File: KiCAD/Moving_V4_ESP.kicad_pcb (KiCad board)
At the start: 2 copper layers, 38 x 63 mm, 48 parts, among them J1 Vin_1, J2 Vin_2, J3 Power_SW, J4 USB_B_Micro, J5 MOTOR_R, J6 Motor_L, SW1 SW_Reset, U1 CH340X, U2 UZ1085L-33-TN3-R, U3 ESP32-WROOM-32, U4 ITR8307-S17-TR8, U5 ITR8307-S17-TR8, U6 ITR8307-S17-TR8, U7 CP2119LDTR, U8 CP2119LDTR

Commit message: Revのテキストを更新
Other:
- board text added: "ESP Mini PF Base Circuit 38 x 63 Rev 0.2"
- board text removed: "ESP Mini PF Base Circuit 38 x 63 Rev 0.1"
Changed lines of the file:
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@@
     (effects (font (size 1 1) (thickness 0.15)) (justify left bottom))
   )
-  (gr_text "ESP Mini PF Base Circuit\n38 x 63\nRev 0.1" (at 108 106) (layer "F.SilkS")
+  (gr_text "ESP Mini PF Base Circuit\n38 x 63\nRev 0.2" (at 108 106) (layer "F.SilkS")
     (effects (font (size 1 1) (thickness 0.15)) (justify left bottom))
   )

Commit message: 主要部品をロック
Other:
- board text added: "locked"
- board text removed: "ESP Mini PF Base Circuit 38 x 63 Rev 0.2"

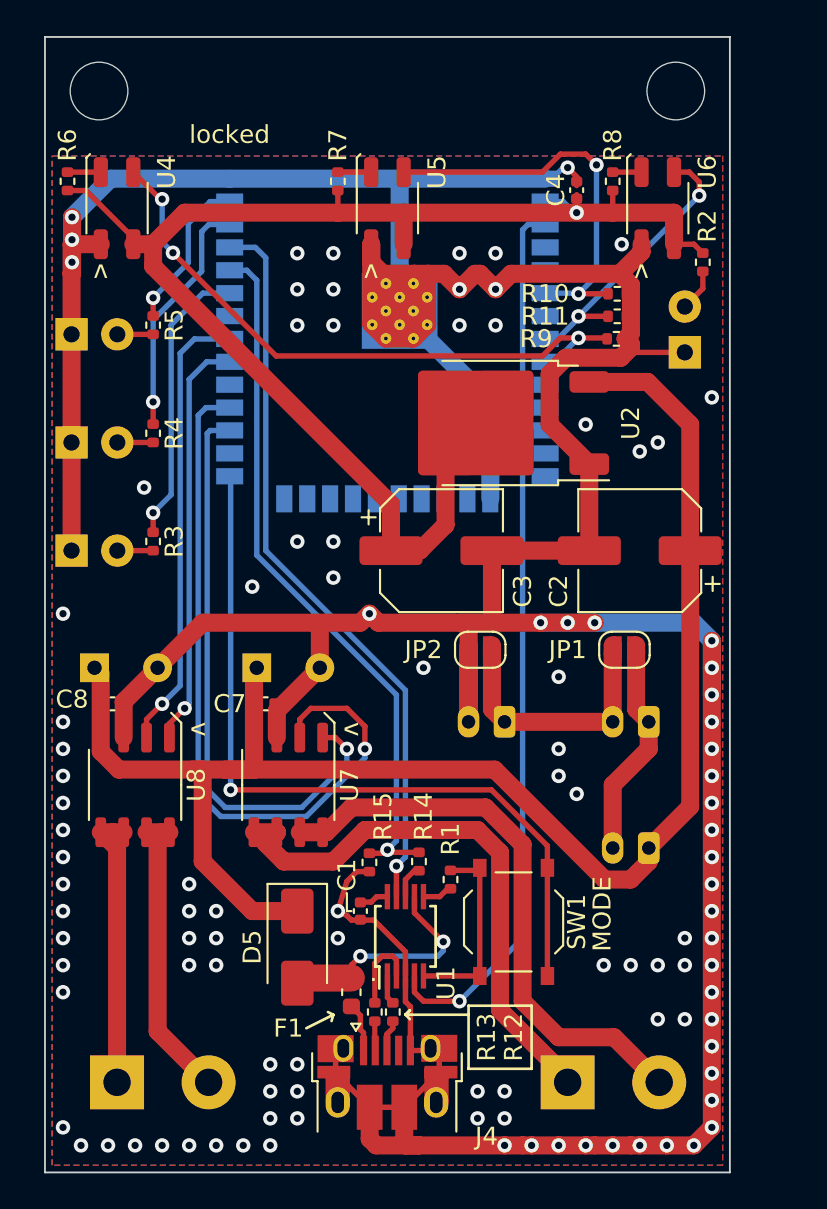
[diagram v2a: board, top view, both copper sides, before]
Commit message: 部品を仮配置
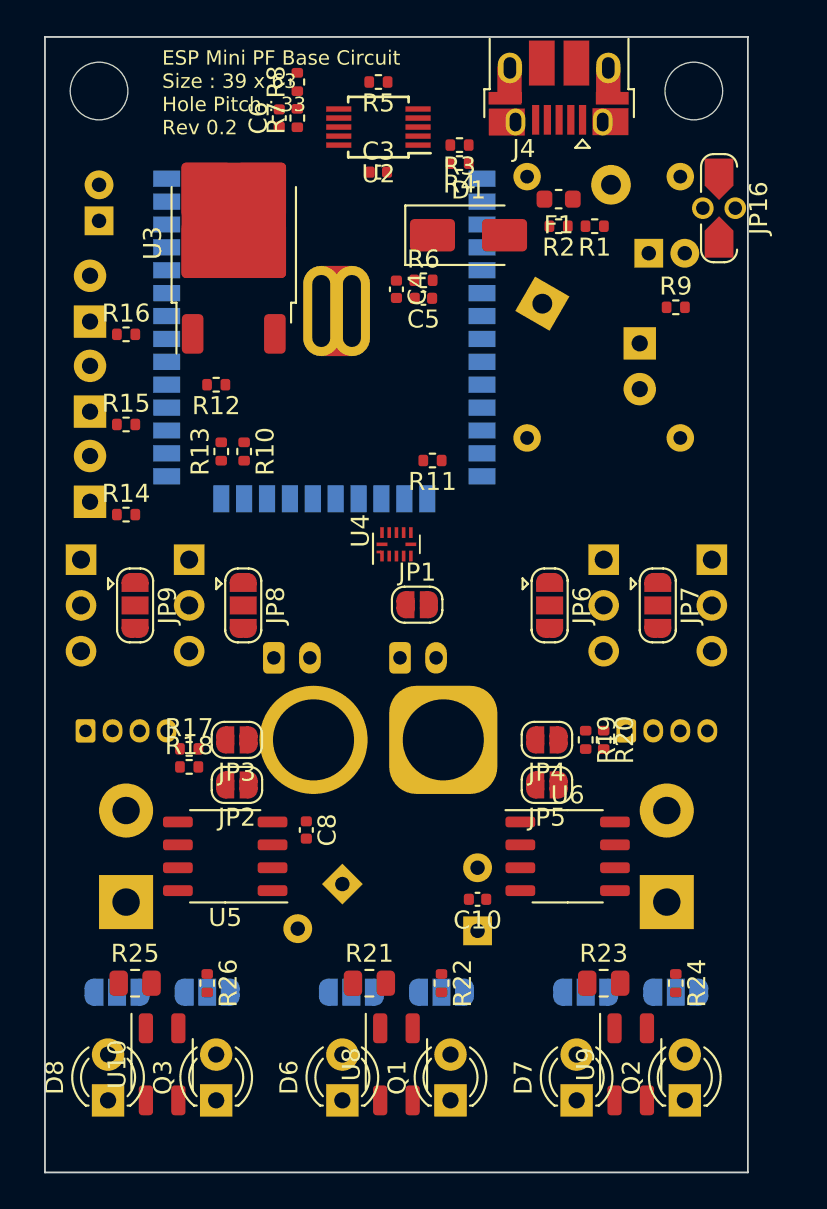
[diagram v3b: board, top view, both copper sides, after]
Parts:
- removed SW1: SW_Reset, Button_Switch_SMD:SW_Push_1P1T_XKB_TS-1187A
- removed the U7 at (113.5, 141.5)
- added C10: 0.1u, Capacitor_SMD:C_0402_1005Metric, F.Cu at (124.0, 147.8)
- added C9: 470u, Capacitor_THT:CP_Radial_D8.0mm_P3.50mm, B.Cu at (124.0, 149.6)
- added D6: U4_ALT1, LED_THT:LED_D3.0mm, F.Cu at (116.5, 159.0)
- added D7: U4_ALT1, LED_THT:LED_D3.0mm, F.Cu at (129.5, 159.0)
- added D8: U4_ALT1, LED_THT:LED_D3.0mm, F.Cu at (103.5, 159.0)
- added J10: IO27_GPIO1, Connector_PinHeader_2.54mm:PinHeader_1x03_P2.54mm_Vertical, B.Cu at (137.0, 129.0)
- added J11: IO32_GPIO2, Connector_PinHeader_2.54mm:PinHeader_1x03_P2.54mm_Vertical, B.Cu at (108.0, 129.0)
- added J12: IO5_GPIO3(PU), Connector_PinHeader_2.54mm:PinHeader_1x03_P2.54mm_Vertical, B.Cu at (102.0, 129.0)
- added J7: MOTOR_L, TerminalBlock:TerminalBlock_bornier-2_P5.08mm, B.Cu at (104.5, 148.0)
- added J8: MOTOR_R, TerminalBlock:TerminalBlock_bornier-2_P5.08mm, B.Cu at (134.5, 148.0)
- added J9: IO4_GPIO0, Connector_PinHeader_2.54mm:PinHeader_1x03_P2.54mm_Vertical, B.Cu at (131.0, 129.0)
- added JP10: LED_SEL1, Jumper:SolderJumper-3_P1.3mm_Open_RoundedPad1.0x1.5mm, B.Cu at (117.0, 153.0)
- added JP11: PT_SEL1, Jumper:SolderJumper-3_P1.3mm_Open_RoundedPad1.0x1.5mm, B.Cu at (122.0, 153.0)
- added JP12: LED_SEL1, Jumper:SolderJumper-3_P1.3mm_Open_RoundedPad1.0x1.5mm, B.Cu at (130.0, 153.0)
- added JP13: PT_SEL1, Jumper:SolderJumper-3_P1.3mm_Open_RoundedPad1.0x1.5mm, B.Cu at (135.0, 153.0)
- added JP14: LED_SEL1, Jumper:SolderJumper-3_P1.3mm_Open_RoundedPad1.0x1.5mm, B.Cu at (104.0, 153.0)
- added JP15: PT_SEL1, Jumper:SolderJumper-3_P1.3mm_Open_RoundedPad1.0x1.5mm, B.Cu at (109.0, 153.0)
- added JP16: Reset, YY_Common:SolderJumper-2_TVAF06-A020B-R_COMPATIBLE, F.Cu at (137.4, 109.5)
- added JP17: USB_Vs, Diode_THT:D_DO-41_SOD81_P7.62mm_Horizontal, B.Cu at (127.6, 114.8)
- added JP3: L2_PU, Jumper:SolderJumper-2_P1.3mm_Open_RoundedPad1.0x1.5mm, F.Cu at (110.7, 139.0)
- added JP4: R1_PU, Jumper:SolderJumper-2_P1.3mm_Open_RoundedPad1.0x1.5mm, F.Cu at (127.8, 139.0)
- added JP5: R2_PU, Jumper:SolderJumper-2_P1.3mm_Open_RoundedPad1.0x1.5mm, F.Cu at (127.8, 141.5)
- added JP6: Vs_SEL0, Jumper:SolderJumper-3_P1.3mm_Open_RoundedPad1.0x1.5mm, F.Cu at (128.0, 131.5)
- added JP7: Vs_SEL1, Jumper:SolderJumper-3_P1.3mm_Open_RoundedPad1.0x1.5mm, F.Cu at (134.0, 131.5)
- added JP8: Vs_SEL2, Jumper:SolderJumper-3_P1.3mm_Open_RoundedPad1.0x1.5mm, F.Cu at (111.0, 131.5)
- added JP9: Vs_SEL3, Jumper:SolderJumper-3_P1.3mm_Open_RoundedPad1.0x1.5mm, F.Cu at (105.0, 131.5)
- added Q1: U4_ALT2, LED_THT:LED_D3.0mm, F.Cu at (122.5, 159.0)
- added Q2: U4_ALT2, LED_THT:LED_D3.0mm, F.Cu at (135.5, 159.0)
- added Q3: U4_ALT2, LED_THT:LED_D3.0mm, F.Cu at (109.5, 159.0)
- added R16: 560, Resistor_SMD:R_0402_1005Metric, F.Cu at (104.5, 116.5)
- added R17: 1k, Resistor_SMD:R_0402_1005Metric, F.Cu at (108.0, 139.5)
- added R18: 1k, Resistor_SMD:R_0402_1005Metric, F.Cu at (108.0, 140.5)
- added R19: 1k, Resistor_SMD:R_0402_1005Metric, F.Cu at (130.0, 139.0)
- added R20: 1k, Resistor_SMD:R_0402_1005Metric, F.Cu at (131.0, 139.0)
- added R21: 50, Resistor_SMD:R_0805_2012Metric, F.Cu at (118.0, 152.5)
- added R22: 1k, Resistor_SMD:R_0402_1005Metric, F.Cu at (122.0, 152.5)
- added R23: 50, Resistor_SMD:R_0805_2012Metric, F.Cu at (131.0, 152.5)
- added R24: 1k, Resistor_SMD:R_0402_1005Metric, F.Cu at (135.0, 152.5)
- added R25: 50, Resistor_SMD:R_0805_2012Metric, F.Cu at (105.0, 152.5)
- added R26: 1k, Resistor_SMD:R_0402_1005Metric, F.Cu at (109.0, 152.5)
- added U10: ITR8307-S17-TR8, OptoDevice:Everlight_ITR1201SR10AR, F.Cu at (106.5, 157.0)
- added U3: UZ1085L-33-TN3-R, Package_TO_SOT_SMD:TO-252-2, F.Cu at (110.5, 111.4)
- added U9: ITR8307-S17-TR8, OptoDevice:Everlight_ITR1201SR10AR, F.Cu at (132.5, 157.0)
- C1: value 0.1u -> 22u; footprint Capacitor_SMD:C_0402_1005Metric -> Capacitor_THT:CP_Radial_D5.0mm_P2.00mm; moved to B.Cu
- C2: footprint Capacitor_SMD:CP_Elec_6.3x5.4 -> Capacitor_THT:CP_Radial_D5.0mm_P2.00mm; moved to B.Cu
- C3: value 22u -> 0.1u; footprint Capacitor_SMD:CP_Elec_6.3x5.4 -> Capacitor_SMD:C_0402_1005Metric
- C5: value 470u -> 10u; footprint Capacitor_THT:CP_Radial_D8.0mm_P3.50mm -> Capacitor_SMD:C_0402_1005Metric; moved to F.Cu
- C6: value 470u -> 20p; footprint Capacitor_THT:CP_Radial_D8.0mm_P3.50mm -> Capacitor_SMD:C_0402_1005Metric; moved to F.Cu
- C7: value 0.1u -> 470u; footprint Capacitor_SMD:C_0402_1005Metric -> Capacitor_THT:CP_Radial_D8.0mm_P3.50mm; moved to B.Cu
- D1: value LED_POWER -> CDBA240LL-HF; footprint LED_THT:LED_D3.0mm -> Diode_SMD:D_SMA; moved to F.Cu
- D2: value LED_R -> LED_POWER
- D3: value LED_Y -> LED_R
- D4: value LED_G -> LED_Y
- D5: value CDBA240LL-HF -> LED_G; footprint Diode_SMD:D_SMA -> LED_THT:LED_D3.0mm; moved to B.Cu
- J2: value Vin_2 -> Power_SW
- J3: value Power_SW -> Vin_XT; footprint Connector_JST:JST_PH_B2B-PH-K_1x02_P2.00mm_Vertical -> Connector_AMASS:AMASS_XT60-M_1x02_P7.20mm_Vertical
- J5: value MOTOR_R -> Encorder_L; footprint TerminalBlock:TerminalBlock_bornier-2_P5.08mm -> YY_Common:JST_ZH_B4B-ZH-A_1x04_P1.50mm_Vertical
- J6: value Motor_L -> Encorder_R; footprint TerminalBlock:TerminalBlock_bornier-2_P5.08mm -> YY_Common:JST_ZH_B4B-ZH-A_1x04_P1.50mm_Vertical
- JP1: value Vin_2_DIisable -> Power_SW_DIisable
- JP2: value Power_SW_DIisable -> L1_PU
- R1: value 4.7k -> 18k
- R12, R13: value 22 -> 1k
- R15, R9: value 1k -> 560
- R2: value 560 -> 2k
- R3, R4: value 560 -> 22
- R5: value 560 -> 4.7k
- R6, R8: value 150 -> 1k
- R7: value 150 -> 560
- U1: value CH340X -> CN39033A; footprint Package_SO:MSOP-10_3x3mm_P0.5mm -> YY_Common:DCDC_Conv_CN39033A; moved to B.Cu
- U2: value UZ1085L-33-TN3-R -> CH340X; footprint Package_TO_SOT_SMD:TO-252-2 -> Package_SO:MSOP-10_3x3mm_P0.5mm
- U4: value ITR8307-S17-TR8 -> TXB0104RUT; footprint OptoDevice:Everlight_ITR1201SR10AR -> Package_DFN_QFN:Texas_R-PUQFN-N12
- U5, U6: value ITR8307-S17-TR8 -> CP3119MDTR; footprint OptoDevice:Everlight_ITR1201SR10AR -> Package_SO:SOP-8_3.9x4.9mm_P1.27mm
- U7: renamed from U3; footprint RF_Module:ESP32-WROOM-32 -> YY_Common:ESP32-WROOM-32_39P-TH
- U8: value CP2119LDTR -> ITR8307-S17-TR8; footprint Package_SO:SOP-8_3.9x4.9mm_P1.27mm -> OptoDevice:Everlight_ITR1201SR10AR
- moved J4 56.0 mm to (128.5, 102.8), turned to 180 degrees
- moved F1 45.5 mm to (128.5, 109.0), turned to 180 degrees
- moved C1 39.9 mm to (133.5, 112.0), turned to 0 degrees
- moved R1 37.1 mm to (130.5, 110.5), turned to 180 degrees
- moved U5 37.1 mm to (110.0, 145.5), turned to 180 degrees
- moved U1 36.6 mm to (131.0, 115.0)
- moved D5 36.6 mm to (102.5, 115.8), turned to 90 degrees
- moved U6 36.3 mm to (129.0, 145.5)
- moved R12 36.2 mm to (109.5, 119.3), turned to 180 degrees
- moved C2 35.1 mm to (103.0, 110.2), turned to 90 degrees
- moved D2 33.6 mm to (133.0, 117.0), turned to -90 degrees
- moved R13 32.2 mm to (109.8, 123.0)
- moved C6 32.2 mm to (113.0, 104.5), turned to 90 degrees
- moved R15 27.8 mm to (104.5, 121.5), turned to 0 degrees
- moved R3 27.8 mm to (123.0, 106.0), turned to 180 degrees
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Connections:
- C1 pad 1: Net-(U1-V3) -> +5V
- C2 pad 1: /Vin -> +3.3V
- C3 pad 1: +3.3V -> Net-(U2-V3)
- C5 pad 1: /Vin -> /EN
- C6 pad 1: /Vin -> /Tx(USB->ESP)
- C6 pad 2: GND -> Net-(U7-RXD0/IO3)
- D1 pad 1: GND -> +5V
- D1 pad 2: Net-(D1-A) -> /USB 5V_F
- D2 pad 1: GND -> Net-(D2-K)
- D2 pad 2: Net-(D2-A) -> +3.3V
- D3 pad 1: GND -> Net-(D3-K)
- D3 pad 2: Net-(D3-A) -> /LED_R
- D4 pad 1: GND -> Net-(D4-K)
- D4 pad 2: Net-(D4-A) -> /LED_Y
- D5 pad 1: /Vin -> Net-(D5-K)
- D5 pad 2: /USB 5V_F -> /LED_G
- J2 pad 2: /P_in2- -> GND
- J3 pad 1: /P_in2- -> GND
- J3 pad 2: GND -> /Vin
- J5 pad 1: /P_MOT_R2 -> +5V
- J5 pad 2: /P_MOT_R1 -> Net-(J5-Pin_2)
- J6 pad 1: /P_MOT_L2 -> +5V
- J6 pad 2: /P_MOT_L1 -> Net-(J6-Pin_2)
- JP1 pad 2: /P_in2- -> GND
- JP2 pad 1: /P_in2- -> Net-(J5-Pin_2)
- JP2 pad 2: GND -> Net-(JP2-B)
- R1 pad 1: Net-(U1-~{CTS}) -> /Vin
- R1 pad 2: Net-(U1-TNOW/~{DTR}) -> /Vs_monitor
- R10 pad 1: /SENSOR_2 -> +3.3V
- R10 pad 2: GND -> /MTDO
- R11 pad 1: /SENSOR_3 -> /MTDI
- R12 pad 1: /D+ -> +3.3V
- R12 pad 2: Net-(U1-UD+) -> /Debug Log
- R13 pad 1: /D- -> /DL Boot
- R13 pad 2: Net-(U1-UD-) -> GND
- R14 pad 1: /Tx(USB->ESP) -> Net-(D3-K)
- R14 pad 2: Net-(U3-RXD0/IO3) -> GND
- R15 pad 1: Net-(U3-RXD0/IO3) -> Net-(D4-K)
- R2 pad 1: +3.3V -> /Vs_monitor
- R2 pad 2: Net-(D1-A) -> GND
- R3 pad 1: /LED_R -> /D+
- R3 pad 2: Net-(D2-A) -> Net-(U2-UD+)
- R4 pad 1: /LED_Y -> /D-
- R4 pad 2: Net-(D3-A) -> Net-(U2-UD-)
- R5 pad 1: /LED_G -> /IO_0
- R5 pad 2: Net-(D4-A) -> Net-(U2-TNOW/~{DTR})
- R6 pad 1: Net-(U4-A) -> +3.3V
- R6 pad 2: +3.3V -> /EN
- R7 pad 1: Net-(U5-A) -> /Tx(USB->ESP)
- R7 pad 2: +3.3V -> Net-(U7-RXD0/IO3)
- R8 pad 1: Net-(U6-A) -> Net-(U7-RXD0/IO3)
- R8 pad 2: +3.3V -> GND
- R9 pad 1: /SENSOR_1 -> Net-(D2-K)
- U1 pad 1: Net-(U1-UD+) -> /Vin
- U1 pad 2: Net-(U1-UD-) -> GND
- U1 pad 4: /EN -> +5V
- U2 pad 1: GND -> Net-(U2-UD+)
- U2 pad 2: +3.3V -> Net-(U2-UD-)
- U2 pad 3: /Vin -> GND
- U4 pad 1: GND -> +3.3V
- U4 pad 2: Net-(U4-A) -> /ENC_L1
- U4 pad 3: +3.3V -> /ENC_L2
- U4 pad 4: /SENSOR_1 -> /ENC_R1
- U5 pad 1: GND -> /L_in1
- U5 pad 2: Net-(U5-A) -> /L_in2
- U5 pad 3: +3.3V -> GND
- U5 pad 4: /SENSOR_2 -> /Vin
- U6 pad 1: GND -> /R_in1
- U6 pad 2: Net-(U6-A) -> /R_in2
- U6 pad 3: +3.3V -> GND
- U6 pad 4: /SENSOR_3 -> /Vin
- U7 pad 10: unconnected-(U3-IO25-Pad10) -> /ENC_R1
- U7 pad 11: unconnected-(U3-IO26-Pad11) -> /ENC_R2
- U7 pad 12: unconnected-(U3-IO27-Pad12) -> /GPIO_1
- U7 pad 13: unconnected-(U3-IO14-Pad13) -> /ENC_L2
- U7 pad 14: unconnected-(U3-IO12-Pad14) -> /MTDI
- U7 pad 16: unconnected-(U3-IO13-Pad16) -> /ENC_L1
- U7 pad 23: unconnected-(U3-IO15-Pad23) -> /MTDO
- U7 pad 24: unconnected-(U3-IO2-Pad24) -> /DL Boot
- U7 pad 26: unconnected-(U3-IO4-Pad26) -> /GPIO_0
- U7 pad 29: unconnected-(U3-IO5-Pad29) -> /Debug Log
- U7 pad 34: Net-(U3-RXD0/IO3) -> Net-(U7-RXD0/IO3)
- U7 pad 4: unconnected-(U3-SENSOR_VP-Pad4) -> /Vs_monitor
- U7 pad 7: unconnected-(U3-IO35-Pad7) -> /SENSOR_3
- U7 pad 8: /SENSOR_3 -> /GPIO_2
- U8 pad 1: /R_in1 -> GND
- U8 pad 2: /R_in2 -> Net-(JP10-A)
- U8 pad 3: GND -> +3.3V
- U8 pad 4: /Vin -> Net-(JP11-A)
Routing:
- net GND: track 285.1 -> 0.00 mm, vias 109 -> 0
- net /Vin: track 93.5 -> 0.00 mm
- net +3.3V: track 76.8 -> 0.00 mm, vias 1 -> 0
- net /EN: track 49.2 -> 0.00 mm, vias 1 -> 0
- net /IO_0: track 43.3 -> 0.00 mm, vias 1 -> 0
- net /Rx(USB<-ESP): track 41.1 -> 0.00 mm, vias 1 -> 0
- net /L_in2: track 41.1 -> 0.00 mm, vias 1 -> 0
- net Net-(U3-RXD0/IO3): track 39.6 -> 0.00 mm, vias 1 -> 0
- net /SENSOR_1: track 34.7 -> 0.00 mm, vias 3 -> 0
- net /L_in1: track 32.6 -> 0.00 mm, vias 1 -> 0
- net /P_MOT_L1: track 31.9 -> 0.00 mm
- net /P_MOT_L2: track 31.1 -> 0.00 mm
- net /R_in2: track 25.2 -> 0.00 mm, vias 1 -> 0
- net /R_in1: track 23.0 -> 0.00 mm, vias 1 -> 0
- net /SENSOR_2: track 22.4 -> 0.00 mm, vias 2 -> 0
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- removed copper zone on B.Cu, net GND
- removed copper zone on F.Cu, net GND
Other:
- board size 38 x 63 mm -> 39 x 63 mm
- board text added: "(100,100)"
- board text added: "(100,163)"
- board text added: "(119.5,163)"
- board text added: "(139,100)"
- board text added: "(139,163)"
- board text added: "ESP Mini PF Base Circuit Size : 39 x 63 Hole Pitch : 33 Rev 0.2"
- board text removed: "+"
- board text removed: "-"
- board text removed: "."
- board text removed: "GRN"
- board text removed: "MODE"
- board text removed: "MOTOR_L"
- board text removed: "MOTOR_R"
- board text removed: "POWER"
- board text removed: "RED"
- board text removed: "SW"
- board text removed: "Vin1"
- board text removed: "Vin2"
- board text removed: "YEL"
- board text removed: "locked"
- board text removed: "v"

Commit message: レイアウトを仮配線
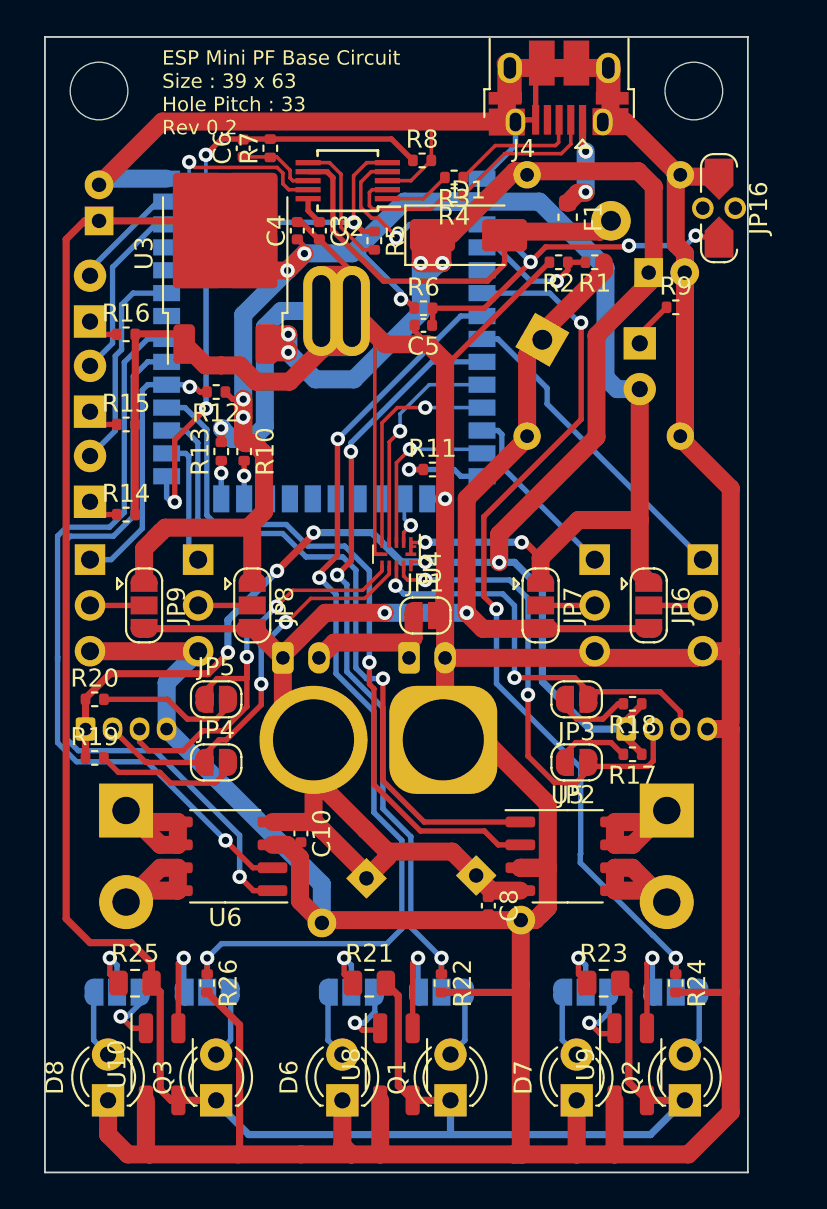
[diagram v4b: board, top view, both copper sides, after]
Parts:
- moved J7 30.4 mm to (134.5, 142.9), turned to -90 degrees
- moved J8 30.4 mm to (104.5, 142.9), turned to -90 degrees
- moved J5 30.0 mm to (132.2, 138.4)
- moved J6 30.0 mm to (102.2, 138.4)
- moved R20 28.3 mm to (102.8, 136.8), turned to 0 degrees
- moved R19 27.3 mm to (102.8, 140.0), turned to 0 degrees
- moved R18 24.8 mm to (132.6, 137.0), turned to 180 degrees
- moved R17 24.6 mm to (132.6, 139.8), turned to 180 degrees
- moved U5 19.0 mm to (129.0, 145.5), turned to 0 degrees
- moved U6 19.0 mm to (110.0, 145.5), turned to 180 degrees
- moved JP3 19.0 mm to (129.5, 136.8)
- moved JP5 19.0 mm to (109.5, 136.8), turned to 0 degrees
- moved JP2 18.9 mm to (129.5, 140.2)
- moved JP4 18.4 mm to (109.5, 140.2), turned to 0 degrees
- moved C8 10.9 mm to (124.6, 148.2)
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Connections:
- U7 pad 26: /GPIO_0 -> /GPIO_2
- U7 pad 8: /GPIO_2 -> /GPIO_0
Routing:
- net GND: track 0.00 -> 380.8 mm, vias 0 -> 2
- net +3.3V: track 0.00 -> 215.9 mm, vias 0 -> 7
- net +5V: track 0.00 -> 114.6 mm, vias 0 -> 9
- net /Vin: track 0.00 -> 88.6 mm, vias 0 -> 2
- net /SENSOR_3: track 0.00 -> 54.6 mm, vias 0 -> 3
- net /SENSOR_2: track 0.00 -> 51.2 mm, vias 0 -> 3
- net /SENSOR_1: track 0.00 -> 43.2 mm, vias 0 -> 3
- net /R_in2: track 0.00 -> 41.9 mm, vias 0 -> 1
- net /R_in1: track 0.00 -> 41.5 mm, vias 0 -> 1
- net /L_in2: track 0.00 -> 39.3 mm, vias 0 -> 1
- net /L_in1: track 0.00 -> 37.6 mm, vias 0 -> 1
- net /EN: track 0.00 -> 33.6 mm, vias 0 -> 4
- net /IO_0: track 0.00 -> 31.2 mm, vias 0 -> 3
- net /USB 5V_F: track 0.00 -> 29.1 mm
- net Net-(J5-Pin_2): track 0.00 -> 27.0 mm, vias 0 -> 2
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
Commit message: 基本的なシルクを配置
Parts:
- moved C6 0.10 mm to (111.0, 106.1)
- moved R7 0.10 mm to (112.5, 106.1)
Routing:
- net GND: track 380.8 -> 375.3 mm
- net +5V: track 114.6 -> 112.3 mm
- net /EN: track 33.6 -> 33.0 mm
- net Net-(J6-Pin_3): track 26.0 -> 25.3 mm
- net /Vin: track 88.6 -> 88.0 mm

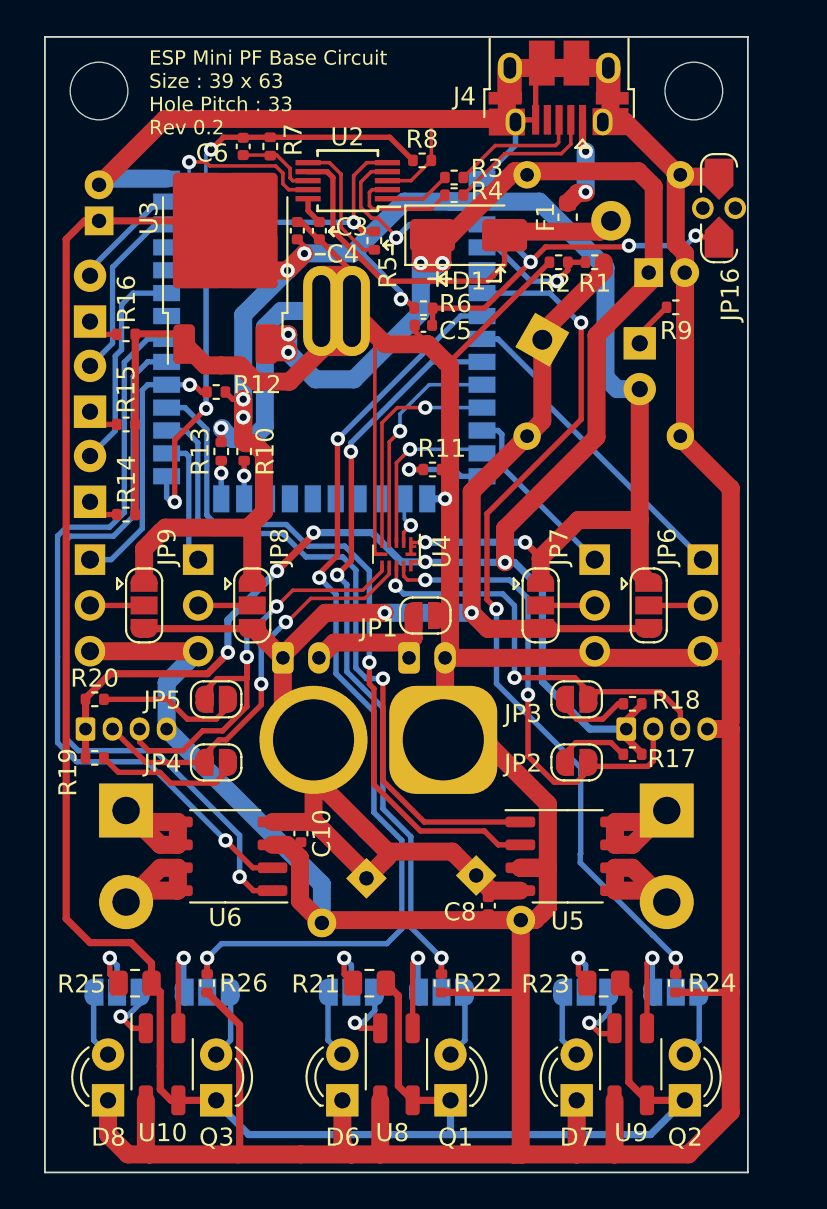
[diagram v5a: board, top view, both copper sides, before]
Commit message: シルク・塗りつぶりを調整
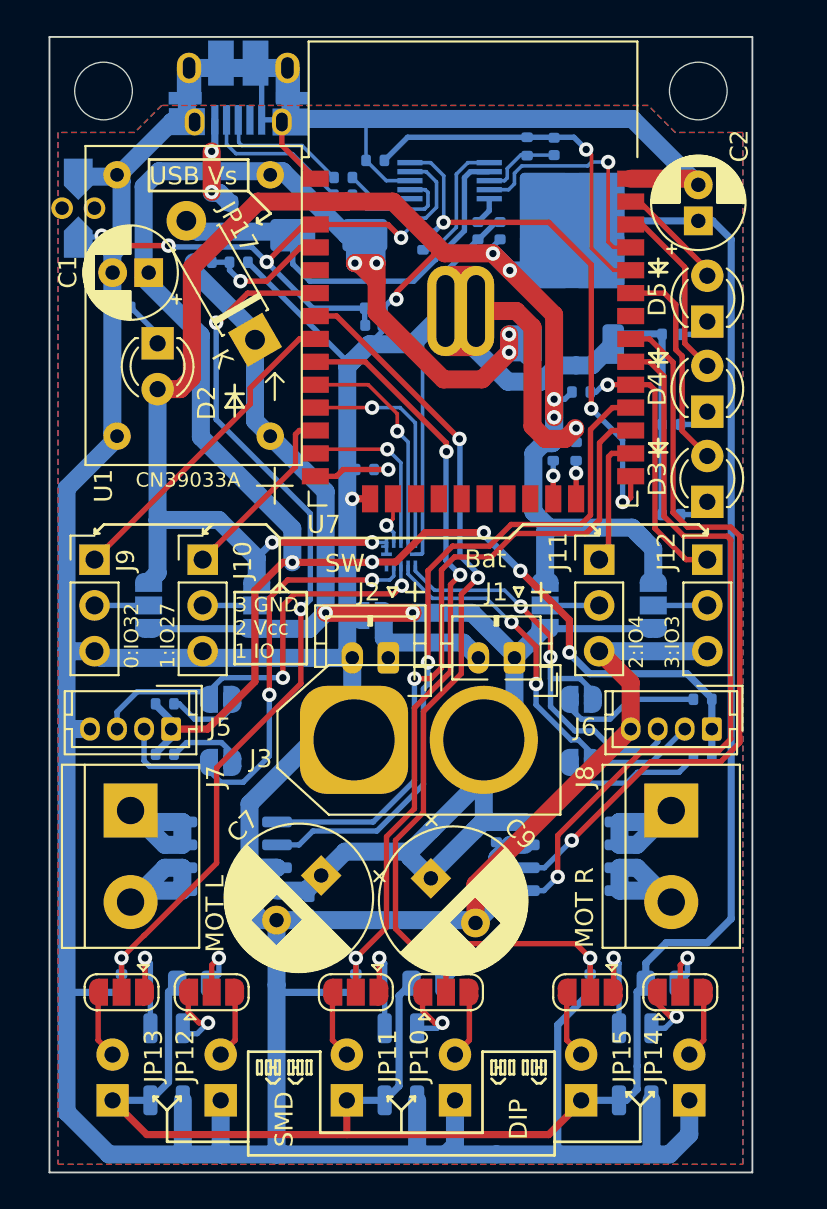
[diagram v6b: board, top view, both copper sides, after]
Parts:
- C1, C2, C7, C9, D2, D3, D4, D5, J1, J10, J11, J12, J2, J3, J5, J6, J7, J8, J9, JP10, JP11, JP12, JP13, JP14, JP15, JP17, U1, U7: moved to F.Cu
- C10, C3, C4, C5, C6, C8, D1, D6, D7, D8, F1, J4, JP1, JP16, JP2, JP3, JP4, JP5, JP6, JP7, JP8, JP9, Q1, Q2, Q3, R1, R10, R11, R12, R13, R14, R15, R16, R17, R18, R19, R2, R20, R21, R22, R23, R24, R25, R26, R3, R4, R5, R6, R7, R8, R9, REF** (x2), U10, U2, U3, U4, U5, U6, U8, U9: moved to B.Cu
- moved JP16 35.6 mm to (101.8, 109.5)
- moved J6 34.7 mm to (137.0, 138.4), turned to 180 degrees
- moved D3 34.2 mm to (136.7, 125.8)
- moved D4 34.2 mm to (136.7, 120.8)
- moved D5 34.2 mm to (136.7, 115.8)
- moved J12 34.2 mm to (136.7, 129.0), turned to 0 degrees
- moved J9 33.8 mm to (102.7, 129.0), turned to 0 degrees
- moved R19 33.7 mm to (136.5, 140.0), turned to 180 degrees
- moved R20 33.7 mm to (136.5, 136.8), turned to 180 degrees
- moved C2 33.2 mm to (136.2, 110.2)
- moved REF** 33.2 mm to (136.2, 103.0), turned to 180 degrees
- moved REF** 32.8 mm to (103.2, 103.0), turned to 180 degrees
- moved D8 32.2 mm to (135.7, 159.0)
- moved Q2 31.8 mm to (103.7, 159.0)
- moved JP14 31.2 mm to (135.2, 153.0), turned to 0 degrees
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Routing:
- added copper zone on B.Cu, net GND
- added copper zone on F.Cu, net GND
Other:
- board text added: "0:IO32"
- board text added: "1:IO27"
- board text added: "2:IO4"
- board text added: "3 GND 2 Vcc 1 IO"
- board text added: "3:IO3"
- board text added: "Bat"
- board text added: "CN39033A"
- board text added: "DIP"
- board text added: "ENC PULLUP"
- board text added: "IH 3.3V HI Vin"
- board text added: "MOT L"
- board text added: "MOT R"
- board text added: "RESET"
- board text added: "SMD"
- board text added: "SW"
- board text added: "SW DISABLE"
- board text added: "USB Vs"

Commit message: 版を記入
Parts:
- C1, C2, C7, C9, D2, D3, D4, D5, J1, J10, J11, J12, J2, J3, J5, J6, J7, J8, J9, JP10, JP11, JP12, JP13, JP14, JP15, JP17, U1, U7: moved to B.Cu
- C10, C3, C4, C5, C6, C8, D1, D6, D7, D8, F1, J4, JP1, JP16, JP2, JP3, JP4, JP5, JP6, JP7, JP8, JP9, Q1, Q2, Q3, R1, R10, R11, R12, R13, R14, R15, R16, R17, R18, R19, R2, R20, R21, R22, R23, R24, R25, R26, R3, R4, R5, R6, R7, R8, R9, REF** (x2), U10, U2, U3, U4, U5, U6, U8, U9: moved to F.Cu
- moved JP16 37.8 mm to (139.7, 109.5)
- moved J9 36.0 mm to (138.8, 129.0), turned to 180 degrees
- moved REF** 35.0 mm to (138.3, 103.0), turned to 0 degrees
- moved Q2 34.0 mm to (137.8, 159.0)
- moved JP13 33.0 mm to (137.3, 153.0), turned to 0 degrees
- moved R24 33.0 mm to (137.3, 152.5)
- moved R9 33.0 mm to (137.3, 115.0), turned to 0 degrees
- moved J6 32.5 mm to (104.5, 138.4), turned to 0 degrees
- moved J7 32.0 mm to (136.8, 142.9)
- moved D3 32.0 mm to (104.8, 125.8)
- moved D4 32.0 mm to (104.8, 120.8)
- moved D5 32.0 mm to (104.8, 115.8)
- moved J12 32.0 mm to (104.8, 129.0), turned to 180 degrees
- moved R19 31.4 mm to (105.1, 140.0), turned to 0 degrees
- moved R20 31.4 mm to (105.1, 136.8), turned to 0 degrees
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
